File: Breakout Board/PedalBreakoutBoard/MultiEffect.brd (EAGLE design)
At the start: 61.9 x 86.3 mm, 65 parts, among them IC1 LD1117V, IC2 MCP6004P, U1 OPA1652AID

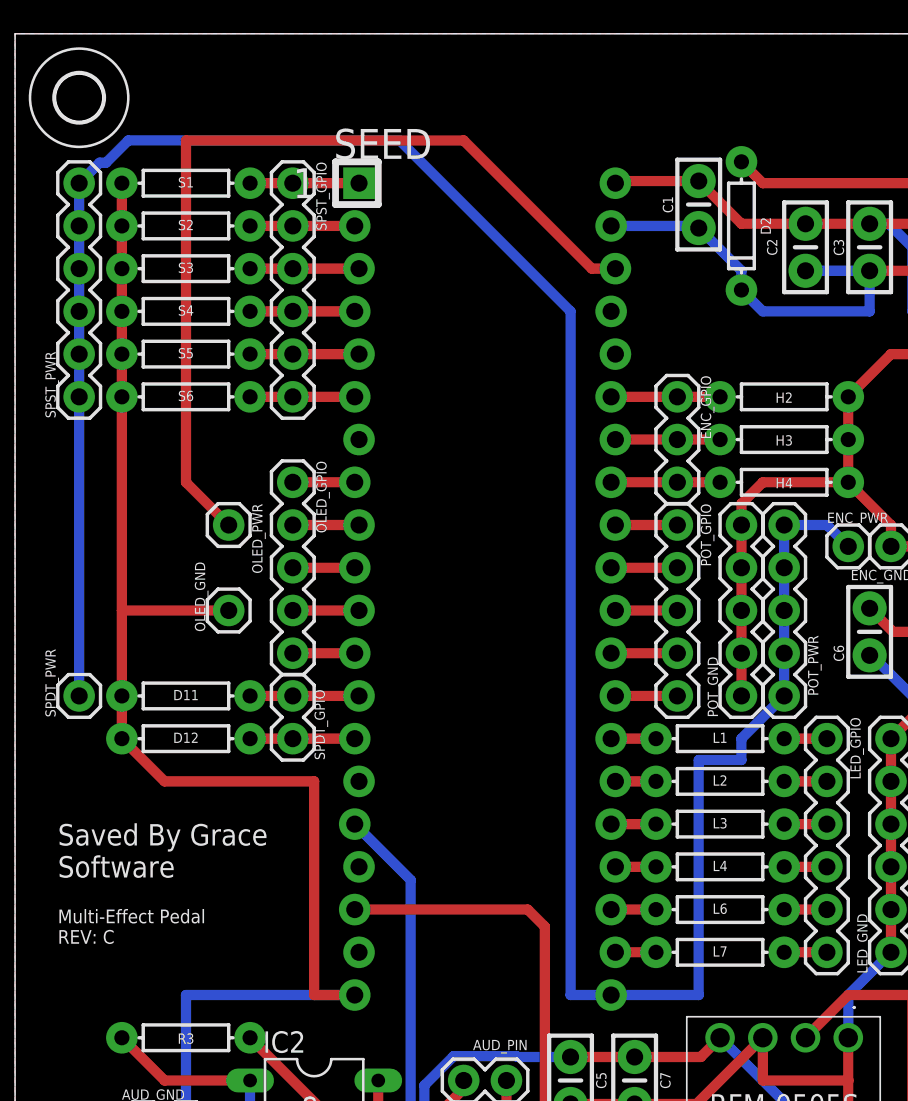
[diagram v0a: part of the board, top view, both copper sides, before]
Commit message: DP-6 - Add additional access to GPIO pins
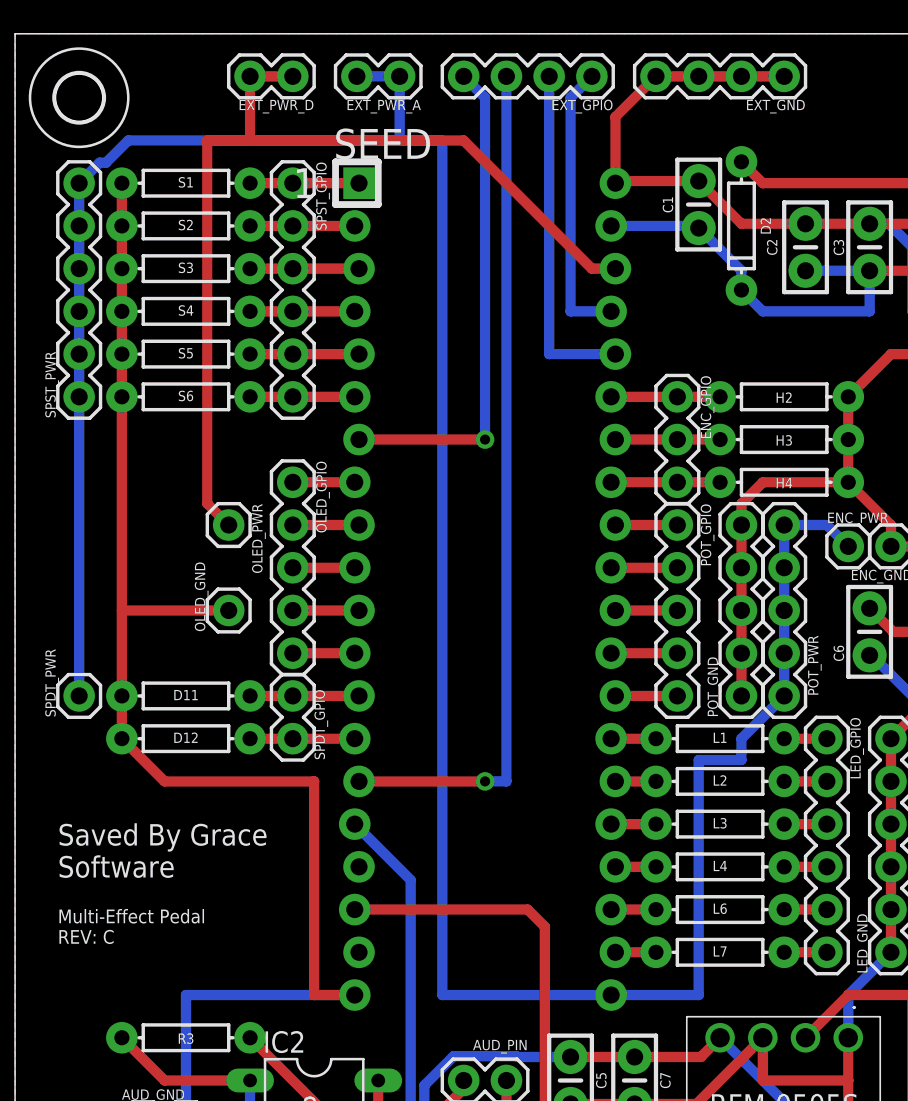
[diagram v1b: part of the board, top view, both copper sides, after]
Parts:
- added EXT_GND, EXT_GPIO: (no value), SparkFun-Connectors:1X04
- added EXT_PWR_A, EXT_PWR_D: (no value), SparkFun-Connectors:1X02
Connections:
- removed net HEX_1: SEED.36
- new net EXT_1: EXT_GPIO.4, SEED.7
- new net EXT_2: EXT_GPIO.3, SEED.15
- new net EXT_3: EXT_GPIO.2, SEED.36
- new net EXT_4: EXT_GPIO.1, SEED.37
- net +3V3_A: now also EXT_PWR_A.1, EXT_PWR_A.2
- net +3V3_D: now also EXT_PWR_D.1, EXT_PWR_D.2
- net GND: now also EXT_GND.1, EXT_GND.2, EXT_GND.3, EXT_GND.4
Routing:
- net EXT_2: track 0.00 -> 50.7 mm, vias 0 -> 1
- net EXT_1: track 0.00 -> 29.6 mm, vias 0 -> 1
- net EXT_3: track 0.00 -> 20.4 mm
- net EXT_4: track 0.00 -> 16.9 mm
- net GND: track 300.8 -> 315.8 mm
- net +3V3_A: track 149.1 -> 161.4 mm
- net +3V3_D: track 52.6 -> 57.1 mm
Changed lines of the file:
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@@
 <attribute name="PROD_ID" value="RES-09435" x="10.16" y="64.77" size="1.778" layer="27" display="off"/>
+</element>
+<element name="EXT_GPIO" library="SparkFun-Connectors" library_urn="urn:adsk.eagle:library:513" package="1X04" package3d_urn="urn:adsk.eagle:package:38085/1" value="" x="34.29" y="83.82" smashed="yes" rot="R180">
+<attribute name="NAME" x="35.56" y="82.423" size="0.6096" layer="25" font="vector" ratio="20" rot="R180"/>
+<attribute name="PROD_ID" value="CONN-09696" x="34.29" y="83.82" size="1.778" layer="27" rot="R180" display="off"/>
+<attribute name="VALUE" x="35.56" y="85.852" size="0.6096" layer="27" font="vector" ratio="20" rot="R180"/>
+</element>
+<element name="EXT_GND" library="SparkFun-Connectors" library_urn="urn:adsk.eagle:library:513" package="1X04" package3d_urn="urn:adsk.eagle:package:38085/1" value="" x="45.72" y="83.82" smashed="yes" rot="R180">
+<attribute name="NAME" x="46.99" y="82.423" size="0.6096" layer="25" font="vector" ratio="20" rot="R180"/>
+<attribute name="PROD_ID" value="CONN-09696" x="45.72" y="83.82" size="1.778" layer="27" rot="R180" display="off"/>
+<attribute name="VALUE" x="46.99" y="85.852" size="0.6096" layer="27" font="vector" ratio="20" rot="R180"/>
+</element>
+<element name="EXT_PWR_A" library="SparkFun-Connectors" library_urn="urn:adsk.eagle:library:513" package="1X02" package3d_urn="urn:adsk.eagle:package:38039/1" value="" x="22.86" y="83.82" smashed="yes" rot="R180">
+<attribute name="NAME" x="24.13" y="82.423" size="0.6096" layer="25" font="vector" ratio="20" rot="R180"/>
+<attribute name="VALUE" x="24.13" y="85.852" size="0.6096" layer="27" font="vector" ratio="20" rot="R180"/>
+</element>
+<element name="EXT_PWR_D" library="SparkFun-Connectors" library_urn="urn:adsk.eagle:library:513" package="1X02" package3d_urn="urn:adsk.eagle:package:38039/1" value="" x="16.51" y="83.82" smashed="yes" rot="R180">
+<attribute name="NAME" x="17.78" y="82.423" size="0.6096" layer="25" font="vector" ratio="20" rot="R180"/>
+<attribute name="VALUE" x="17.78" y="85.852" size="0.6096" layer="27" font="vector" ratio="20" rot="R180"/>
 </element>
 </elements>
@@
 <vertex x="62.23" y="86.36"/>
 </polygon>
+<contactref element="EXT_GND" pad="1"/>
+<contactref element="EXT_GND" pad="2"/>
+<contactref element="EXT_GND" pad="3"/>
+<contactref element="EXT_GND" pad="4"/>
+<wire x1="35.687" y1="77.47" x2="35.687" y2="81.407" width="0.6096" layer="1"/>
+<wire x1="35.687" y1="81.407" x2="38.1" y2="83.82" width="0.6096" layer="1"/>
+<wire x1="38.1" y1="83.82" x2="40.64" y2="83.82" width="0.6096" layer="1"/>
+<wire x1="40.64" y1="83.82" x2="43.18" y2="83.82" width="0.6096" layer="1"/>
+<wire x1="43.18" y1="83.82" x2="45.72" y2="83.82" width="0.6096" layer="1"/>
 </signal>
 <signal name="SPST1">
@@
 <wire x1="39.37" y1="16.637" x2="38.1" y2="15.367" width="0.6096" layer="1"/>
 </signal>
-<signal name="HEX_1">
-<contactref element="SEED" pad="36"/>
-</signal>
 <signal name="ENC_SW">
 <contactref element="SEED" pad="35"/>
@@
 <contactref element="SPDT_PWR" pad="1"/>
 <contactref element="ENC_PWR" pad="1"/>
-<wire x1="22.86" y1="80.01" x2="33.02" y2="69.85" width="0.6096" layer="16"/>
-<wire x1="33.02" y1="69.85" x2="33.02" y2="29.21" width="0.6096" layer="16"/>
-<wire x1="33.02" y1="29.21" x2="35.433" y2="29.21" width="0.6096" layer="16"/>
+<wire x1="25.4" y1="29.21" x2="35.433" y2="29.21" width="0.6096" layer="16"/>
 <contactref element="POT_PWR" pad="1"/>
 <contactref element="POT_PWR" pad="2"/>
@@
 <wire x1="3.81" y1="77.47" x2="5.0292" y2="78.6892" width="0.6096" layer="16"/>
 <wire x1="5.0292" y1="78.6892" x2="5.4092" y2="78.6892" width="0.6096" layer="16"/>
-<wire x1="5.4092" y1="78.6892" x2="6.73" y2="80.01" width="0.6096" layer="16"/>
-<wire x1="6.73" y1="80.01" x2="22.86" y2="80.01" width="0.6096" layer="16"/>
+<wire x1="6.73" y1="80.01" x2="5.4092" y2="78.6892" width="0.6096" layer="16"/>
+<wire x1="25.4" y1="29.21" x2="25.4" y2="80.01" width="0.6096" layer="16"/>
+<wire x1="25.4" y1="80.01" x2="22.86" y2="80.01" width="0.6096" layer="16"/>
+<contactref element="EXT_PWR_A" pad="1"/>
+<contactref element="EXT_PWR_A" pad="2"/>
+<wire x1="22.86" y1="80.01" x2="6.73" y2="80.01" width="0.6096" layer="16"/>
+<wire x1="22.86" y1="80.01" x2="22.86" y2="83.82" width="0.6096" layer="16"/>
+<wire x1="22.86" y1="83.82" x2="20.32" y2="83.82" width="0.6096" layer="16"/>
 </signal>
 <signal name="SPDT1_1">
@@
 <contactref element="OLED_PWR" pad="1"/>
 <contactref element="SEED" pad="38"/>
-<wire x1="12.7" y1="57.15" x2="10.16" y2="59.69" width="0.6096" layer="1"/>
-<wire x1="10.16" y1="80.01" x2="10.16" y2="59.69" width="0.6096" layer="1"/>
+<wire x1="12.7" y1="57.15" x2="11.43" y2="58.42" width="0.6096" layer="1"/>
+<wire x1="11.43" y1="80.01" x2="11.43" y2="58.42" width="0.6096" layer="1"/>
 <wire x1="35.687" y1="72.39" x2="34.29" y2="72.39" width="0.6096" layer="1"/>
-<wire x1="26.67" y1="80.01" x2="10.16" y2="80.01" width="0.6096" layer="1"/>
+<wire x1="26.67" y1="80.01" x2="13.97" y2="80.01" width="0.6096" layer="1"/>
+<wire x1="13.97" y1="80.01" x2="11.43" y2="80.01" width="0.6096" layer="1"/>
 <wire x1="34.29" y1="72.39" x2="26.67" y2="80.01" width="0.6096" layer="1"/>
+<contactref element="EXT_PWR_D" pad="2"/>
+<contactref element="EXT_PWR_D" pad="1"/>
+<wire x1="13.97" y1="80.01" x2="13.97" y2="83.82" width="0.6096" layer="1"/>
+<wire x1="13.97" y1="83.82" x2="16.51" y2="83.82" width="0.6096" layer="1"/>
 </signal>
 <signal name="SCL">
@@
 <wire x1="45.72" y1="31.75" x2="48.26" y2="31.75" width="0.6096" layer="1"/>
 </signal>
+<signal name="EXT_1">
+<contactref element="SEED" pad="7"/>
+<contactref element="EXT_GPIO" pad="4"/>
+<wire x1="20.447" y1="62.23" x2="27.94" y2="62.23" width="0.6096" layer="1"/>
+<via x="27.94" y="62.23" extent="1-16" drill="0.6"/>
+<wire x1="27.94" y1="82.55" x2="26.67" y2="83.82" width="0.6096" layer="16"/>
+<wire x1="27.94" y1="62.23" x2="27.94" y2="82.55" width="0.6096" layer="16"/>
+</signal>
+<signal name="EXT_2">
+<contactref element="SEED" pad="15"/>
+<contactref element="EXT_GPIO" pad="3"/>
+<wire x1="20.447" y1="41.91" x2="27.94" y2="41.91" width="0.6096" layer="1"/>
+<via x="27.94" y="41.91" extent="1-16" drill="0.6"/>
+<wire x1="27.94" y1="41.91" x2="29.21" y2="41.91" width="0.6096" layer="16"/>
+<wire x1="29.21" y1="41.91" x2="29.21" y2="83.82" width="0.6096" layer="16"/>
+</signal>
+<signal name="EXT_3">
+<contactref element="EXT_GPIO" pad="2"/>
+<contactref element="SEED" pad="36"/>
+<wire x1="35.687" y1="67.31" x2="31.75" y2="67.31" width="0.6096" layer="16"/>
+<wire x1="31.75" y1="67.31" x2="31.75" y2="83.82" width="0.6096" layer="16"/>
+</signal>
+<signal name="EXT_4">
+<contactref element="EXT_GPIO" pad="1"/>
+<contactref element="SEED" pad="37"/>
+<wire x1="35.433" y1="69.85" x2="33.02" y2="69.85" width="0.6096" layer="16"/>
+<wire x1="33.02" y1="82.55" x2="34.29" y2="83.82" width="0.6096" layer="16"/>
+<wire x1="33.02" y1="69.85" x2="33.02" y2="82.55" width="0.6096" layer="16"/>
+</signal>
 </signals>

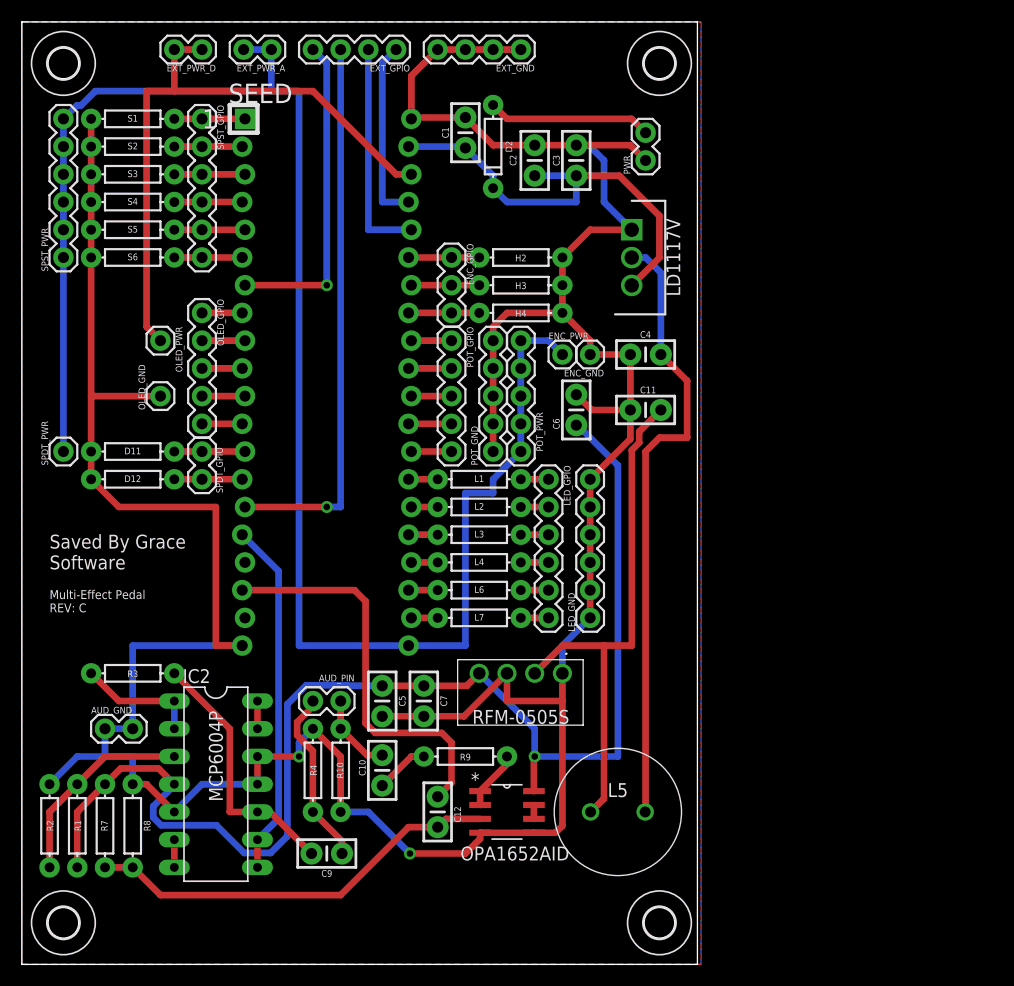
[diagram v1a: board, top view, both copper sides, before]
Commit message: DP-6 - Add logo to board
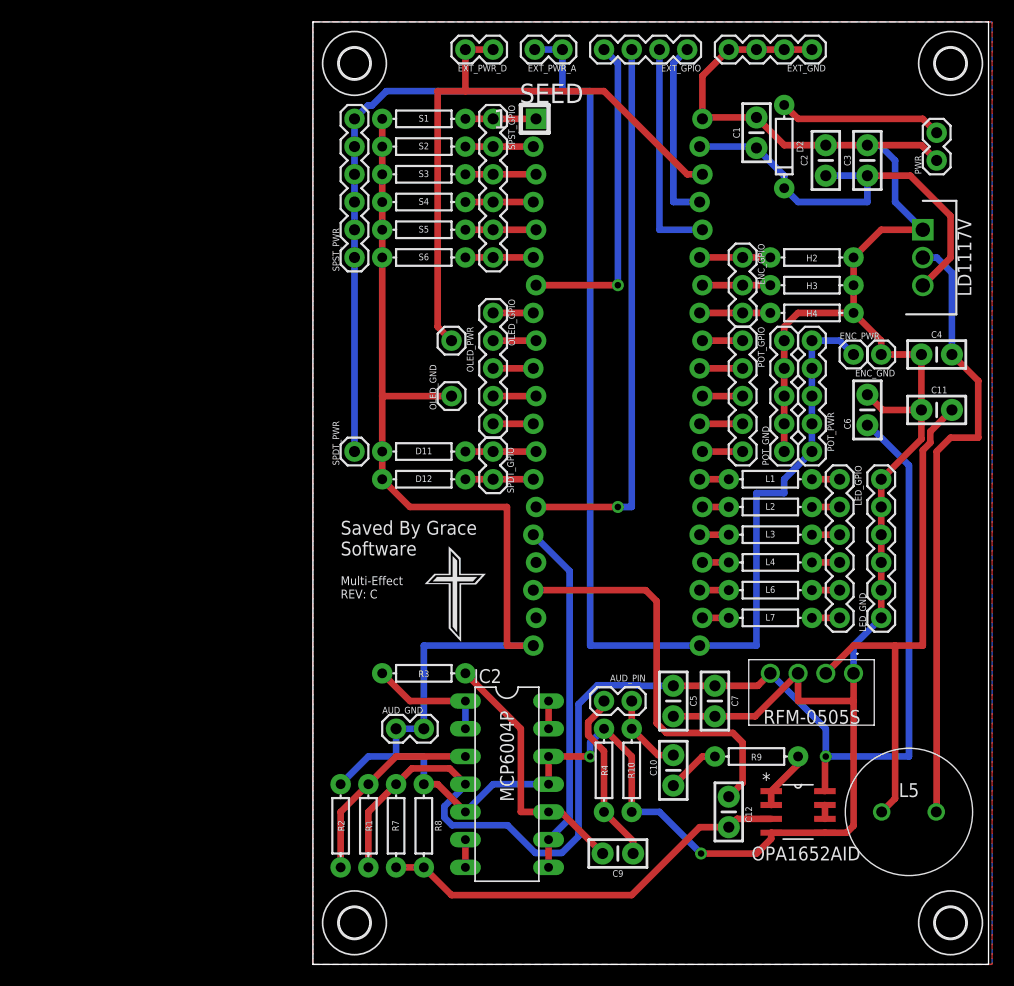
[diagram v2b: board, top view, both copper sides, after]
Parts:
- moved ENC_GPIO 26.7 mm to (66.0, 64.8)
- moved LED_GPIO 26.7 mm to (74.9, 44.5)
- moved POT_GPIO 26.7 mm to (66.0, 57.1)
- moved AUD_PIN 26.7 mm to (55.9, 24.1)
- moved C1 26.7 mm to (67.3, 76.2)
- moved C3 26.7 mm to (77.5, 73.7)
- moved C6 26.7 mm to (77.5, 50.8)
- moved C7 26.7 mm to (63.5, 24.1)
- moved ENC_PWR 26.7 mm to (76.2, 55.9)
- moved EXT_GND 26.7 mm to (72.4, 83.8)
- moved EXT_GPIO 26.7 mm to (61.0, 83.8)
- moved EXT_PWR_A 26.7 mm to (49.5, 83.8)
- moved H2 26.7 mm to (72.4, 64.8)
- moved H3 26.7 mm to (72.4, 62.2)
- moved H4 26.7 mm to (72.4, 59.7)
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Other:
- board text added: "Multi-Effect REV: C"
- board text removed: "Multi-Effect Pedal REV: C"

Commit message: DP-97 - Add schematic for wave analysis board
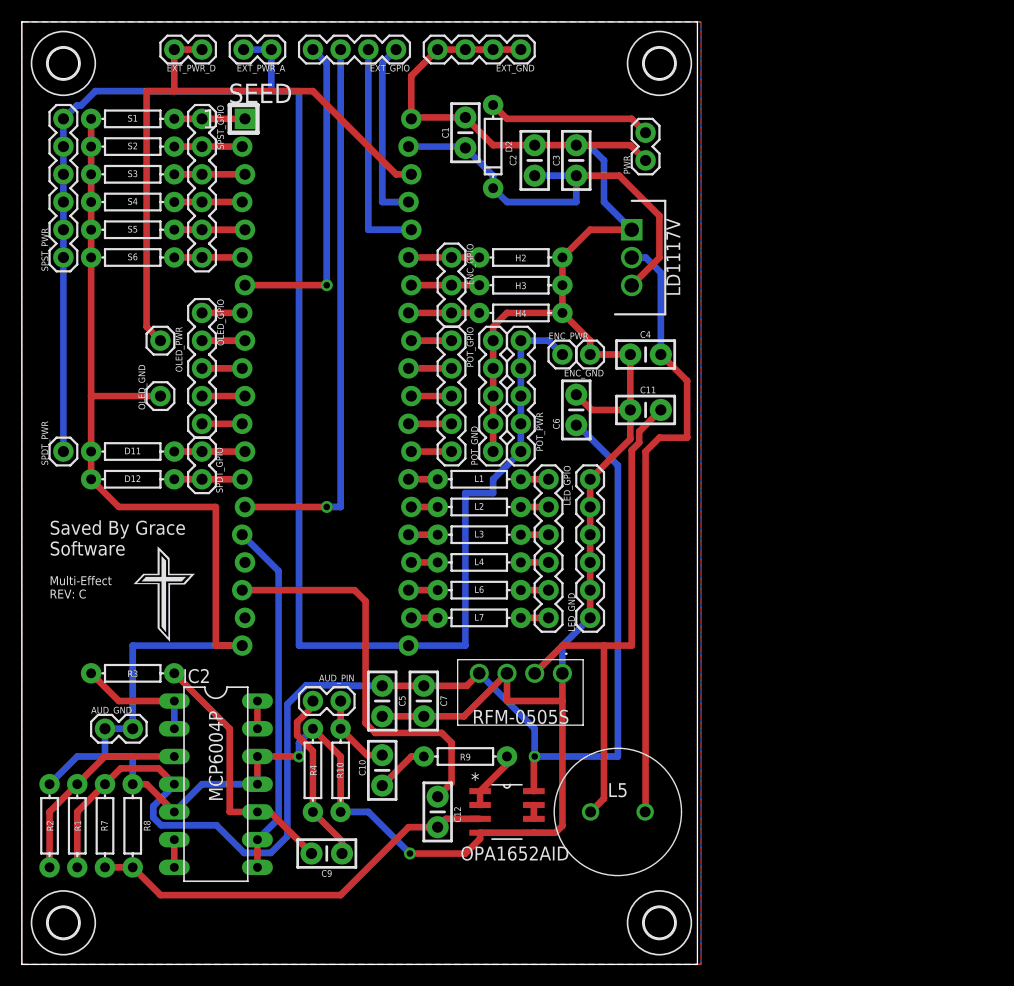
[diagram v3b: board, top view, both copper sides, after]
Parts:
- moved ENC_GPIO 26.7 mm to (39.4, 64.8)
- moved LED_GPIO 26.7 mm to (48.3, 44.5)
- moved POT_GPIO 26.7 mm to (39.4, 57.1)
- moved AUD_PIN 26.7 mm to (29.2, 24.1)
- moved C1 26.7 mm to (40.6, 76.2)
- moved C3 26.7 mm to (50.8, 73.7)
- moved C6 26.7 mm to (50.8, 50.8)
- moved C7 26.7 mm to (36.8, 24.1)
- moved ENC_PWR 26.7 mm to (49.5, 55.9)
- moved EXT_GND 26.7 mm to (45.7, 83.8)
- moved EXT_GPIO 26.7 mm to (34.3, 83.8)
- moved EXT_PWR_A 26.7 mm to (22.9, 83.8)
- moved H2 26.7 mm to (45.7, 64.8)
- moved H3 26.7 mm to (45.7, 62.2)
- moved H4 26.7 mm to (45.7, 59.7)
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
